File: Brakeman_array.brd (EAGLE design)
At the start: 103.1 x 99.1 mm, 56 parts

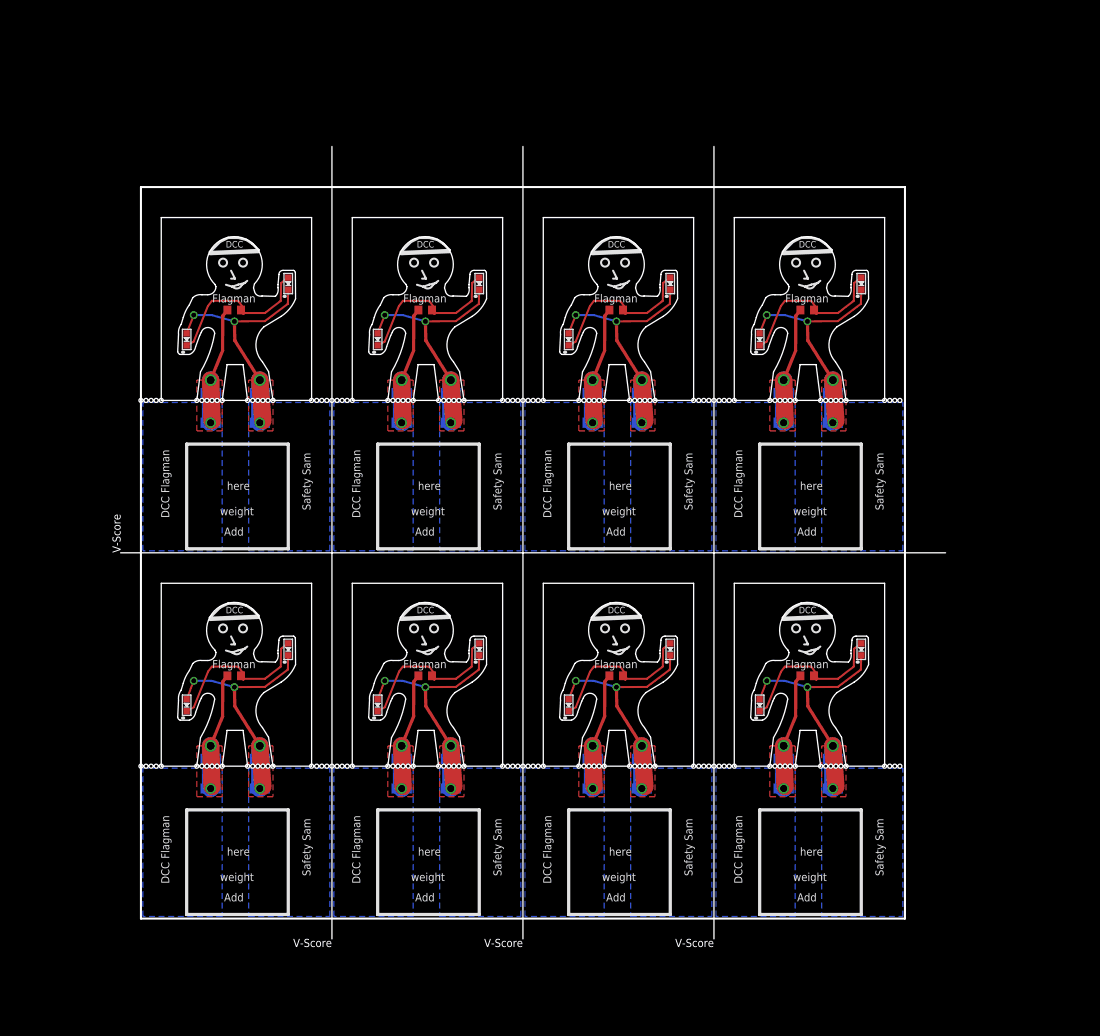
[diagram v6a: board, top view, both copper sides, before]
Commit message: Revert "Version 2.4"
This reverts commit de817f9b6bc09cb4258c25781ce6263bd1cc7bce.
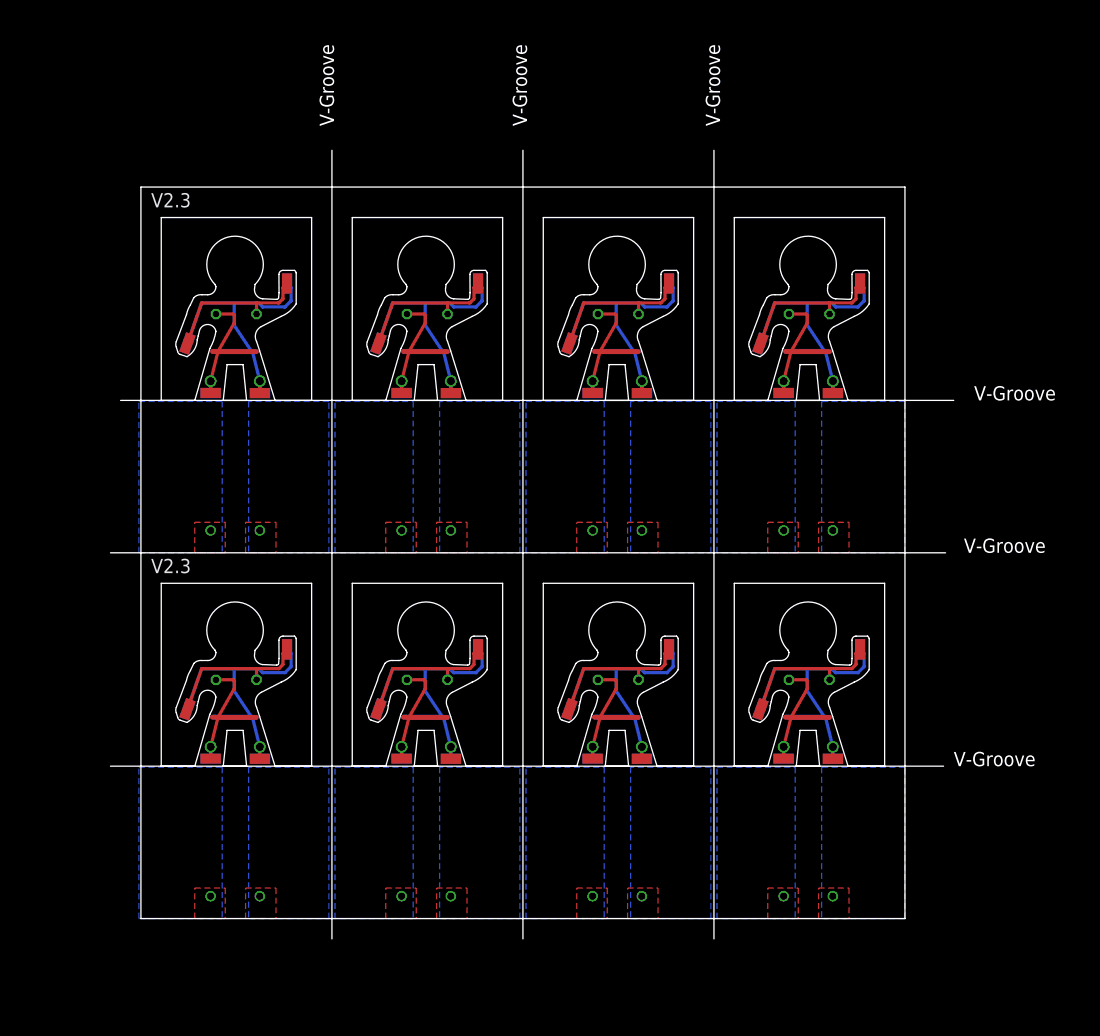
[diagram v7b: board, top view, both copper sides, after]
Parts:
- removed LED1X11, LED1X12, LED1X21, LED1X22, LED1X31, LED1X32, LED1X41, LED1X42, LED2X11, LED2X12, LED2X21, LED2X22, LED2X31, LED2X32, LED2X41, LED2X42: (no value), SPCoast:0603-LED
- removed PADNF1X11, PADNF1X12, PADNF1X21, PADNF1X22, PADNF1X31, PADNF1X32, PADNF1X41, PADNF1X42, PADNFX11, PADNFX12, PADNFX21, PADNFX22, PADNFX31, PADNFX32, PADNFX41, PADNFX42, PADSF1X11, PADSF1X12, PADSF1X21, PADSF1X22, PADSF1X31, PADSF1X32, PADSF1X41, PADSF1X42, PADSFX11, PADSFX12, PADSFX21, PADSFX22, PADSFX31, PADSFX32, PADSFX41, PADSFX42: pad, SPCoast:SMD1,27-2,54
- removed R1KX11, R1KX12, R1KX21, R1KX22, R1KX31, R1KX32, R1KX41, R1KX42: 1k0, resistor:R0603
- added PADL1, PADL10, PADL11, PADL12, PADL13, PADL14, PADL15, PADL16, PADL2, PADL3, PADL4, PADL5, PADL6, PADL7, PADL8, PADL9, PADNA, PADNA1, PADNA10, PADNA11, PADNA12, PADNA13, PADNA14, PADNA15, PADNA2, PADNA3, PADNA4, PADNA5, PADNA6, PADNA7, PADNA8, PADNA9, PADNF, PADNF1, PADNF10, PADNF11, PADNF12, PADNF13, PADNF14, PADNF15, PADNF2, PADNF3, PADNF4, PADNF5, PADNF6, PADNF7, PADNF8, PADNF9, PADSF, PADSF1, PADSF10, PADSF11, PADSF12, PADSF13, PADSF14, PADSF15, PADSF2, PADSF3, PADSF4, PADSF5, PADSF6, PADSF7, PADSF8, PADSF9: pad, wirepad:SMD1.27-2.54
- added R1, R2, R3, R4, R5, R6, R7, R8: 1k0, resistor:0204/5
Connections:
- removed net LIMITEDX11: LED1X11.C, LED2X11.A, R1KX11.1
- removed net LIMITEDX12: LED1X12.C, LED2X12.A, R1KX12.1
- removed net LIMITEDX21: LED1X21.C, LED2X21.A, R1KX21.1
- removed net LIMITEDX22: LED1X22.C, LED2X22.A, R1KX22.1
- removed net LIMITEDX31: LED1X31.C, LED2X31.A, R1KX31.1
- removed net LIMITEDX32: LED1X32.C, LED2X32.A, R1KX32.1
- removed net LIMITEDX41: LED1X41.C, LED2X41.A, R1KX41.1
- removed net LIMITEDX42: LED1X42.C, LED2X42.A, R1KX42.1
- removed net NX11: LED1X11.A, LED2X11.C, PADNF1X11.1, PADNFX11.1
- removed net NX12: LED1X12.A, LED2X12.C, PADNF1X12.1, PADNFX12.1
- removed net NX21: LED1X21.A, LED2X21.C, PADNF1X21.1, PADNFX21.1
- removed net NX22: LED1X22.A, LED2X22.C, PADNF1X22.1, PADNFX22.1
- removed net NX31: LED1X31.A, LED2X31.C, PADNF1X31.1, PADNFX31.1
- removed net NX32: LED1X32.A, LED2X32.C, PADNF1X32.1, PADNFX32.1
- removed net NX41: LED1X41.A, LED2X41.C, PADNF1X41.1, PADNFX41.1
- removed net NX42: LED1X42.A, LED2X42.C, PADNF1X42.1, PADNFX42.1
- removed net SX11: PADSF1X11.1, PADSFX11.1, R1KX11.2
- removed net SX12: PADSF1X12.1, PADSFX12.1, R1KX12.2
- removed net SX21: PADSF1X21.1, PADSFX21.1, R1KX21.2
- removed net SX22: PADSF1X22.1, PADSFX22.1, R1KX22.2
- removed net SX31: PADSF1X31.1, PADSFX31.1, R1KX31.2
- removed net SX32: PADSF1X32.1, PADSFX32.1, R1KX32.2
- removed net SX41: PADSF1X41.1, PADSFX41.1, R1KX41.2
- removed net SX42: PADSF1X42.1, PADSFX42.1, R1KX42.2
- new net LIMITED: PADL1.1, PADL2.1, R1.1
- new net LIMITED1: PADL3.1, PADL4.1, R2.1
- new net LIMITED2: PADL5.1, PADL6.1, R3.1
- new net LIMITED3: PADL7.1, PADL8.1, R4.1
- new net LIMITED4: PADL10.1, PADL9.1, R5.1
- new net LIMITED5: PADL11.1, PADL12.1, R6.1
- new net LIMITED6: PADL13.1, PADL14.1, R7.1
- new net LIMITED7: PADL15.1, PADL16.1, R8.1
- new net N: PADNA.1, PADNA2.1, PADNF.1, PADNF2.1
- new net N1: PADNA1.1, PADNA3.1, PADNF1.1, PADNF3.1
- new net N2: PADNA4.1, PADNA5.1, PADNF4.1, PADNF5.1
- new net N3: PADNA6.1, PADNA7.1, PADNF6.1, PADNF7.1
- new net N4: PADNA8.1, PADNA9.1, PADNF8.1, PADNF9.1
- new net N5: PADNA10.1, PADNA11.1, PADNF10.1, PADNF11.1
- new net N6: PADNA12.1, PADNA13.1, PADNF12.1, PADNF13.1
- new net N7: PADNA14.1, PADNA15.1, PADNF14.1, PADNF15.1
- new net S: PADSF.1, PADSF2.1, R1.2
- new net S1: PADSF1.1, PADSF3.1, R2.2
- new net S2: PADSF4.1, PADSF5.1, R3.2
- new net S3: PADSF6.1, PADSF7.1, R4.2
- new net S4: PADSF8.1, PADSF9.1, R5.2
- new net S5: PADSF10.1, PADSF11.1, R6.2
- new net S6: PADSF12.1, PADSF13.1, R7.2
- new net S7: PADSF14.1, PADSF15.1, R8.2
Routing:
- net N: track 0.00 -> 38.6 mm, vias 0 -> 2
- net N2: track 0.00 -> 38.6 mm, vias 0 -> 2
- net N4: track 0.00 -> 38.6 mm, vias 0 -> 2
- net N6: track 0.00 -> 38.6 mm, vias 0 -> 2
- net N1: track 0.00 -> 38.6 mm, vias 0 -> 2
- net N3: track 0.00 -> 38.6 mm, vias 0 -> 2
- net N5: track 0.00 -> 38.6 mm, vias 0 -> 2
- net N7: track 0.00 -> 38.6 mm, vias 0 -> 2
- net NX42: track 35.5 -> 0.00 mm, vias 4 -> 0
- net NX32: track 35.5 -> 0.00 mm, vias 4 -> 0
- net NX22: track 35.5 -> 0.00 mm, vias 4 -> 0
- net NX12: track 35.5 -> 0.00 mm, vias 4 -> 0
- net NX41: track 35.5 -> 0.00 mm, vias 4 -> 0
- net NX31: track 35.5 -> 0.00 mm, vias 4 -> 0
- net NX21: track 35.5 -> 0.00 mm, vias 4 -> 0
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- added copper zone on layer 1, net N
- added copper zone on layer 16, net N
- added copper zone on layer 1, net N1
- added copper zone on layer 16, net N1
- added copper zone on layer 1, net N2
- added copper zone on layer 16, net N2
- added copper zone on layer 1, net N3
- added copper zone on layer 16, net N3
- added copper zone on layer 1, net N4
- added copper zone on layer 16, net N4
- added copper zone on layer 1, net N5
- added copper zone on layer 16, net N5
- added copper zone on layer 1, net N6
- added copper zone on layer 16, net N6
- added copper zone on layer 1, net N7
- added copper zone on layer 16, net N7
- added copper zone on layer 1, net S
- added copper zone on layer 16, net S
- added copper zone on layer 1, net S1
- added copper zone on layer 16, net S1
- added copper zone on layer 1, net S2
- added copper zone on layer 16, net S2
- added copper zone on layer 1, net S3
- added copper zone on layer 16, net S3
- added copper zone on layer 1, net S4
- added copper zone on layer 16, net S4
- added copper zone on layer 1, net S5
- added copper zone on layer 16, net S5
- added copper zone on layer 1, net S6
- added copper zone on layer 16, net S6
- added copper zone on layer 1, net S7
- added copper zone on layer 16, net S7
- removed copper zone on layer 1, net NX11
- removed copper zone on layer 16, net NX11
- removed copper zone on layer 1, net NX12
- removed copper zone on layer 16, net NX12
- removed copper zone on layer 1, net NX21
- removed copper zone on layer 16, net NX21
- removed copper zone on layer 1, net NX22
- removed copper zone on layer 16, net NX22
- removed copper zone on layer 1, net NX31
- removed copper zone on layer 16, net NX31
- removed copper zone on layer 1, net NX32
- removed copper zone on layer 16, net NX32
- removed copper zone on layer 1, net NX41
- removed copper zone on layer 16, net NX41
- removed copper zone on layer 1, net NX42
- removed copper zone on layer 16, net NX42
- removed copper zone on layer 1, net SX11
- removed copper zone on layer 16, net SX11
- removed copper zone on layer 1, net SX12
- removed copper zone on layer 16, net SX12
- removed copper zone on layer 1, net SX21
- removed copper zone on layer 16, net SX21
- removed copper zone on layer 1, net SX22
- removed copper zone on layer 16, net SX22
- removed copper zone on layer 1, net SX31
- removed copper zone on layer 16, net SX31
- removed copper zone on layer 1, net SX32
- removed copper zone on layer 16, net SX32
- removed copper zone on layer 1, net SX41
- removed copper zone on layer 16, net SX41
- removed copper zone on layer 1, net SX42
- removed copper zone on layer 16, net SX42
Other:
- board size 103.1 x 99.1 mm -> 105.4 x 98.6 mm
- board text added: "2016.11"
- board text added: "Break off and discard"
- board text added: "V-Groove"
- board text added: "V2.3"
- board text removed: "2016.11 2024.01"
- board text removed: "John Plocher 2024.01"
- board text removed: "Safety Sam DCC Flagman"
- board text removed: "V-Score"

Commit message: added foot tiedowns
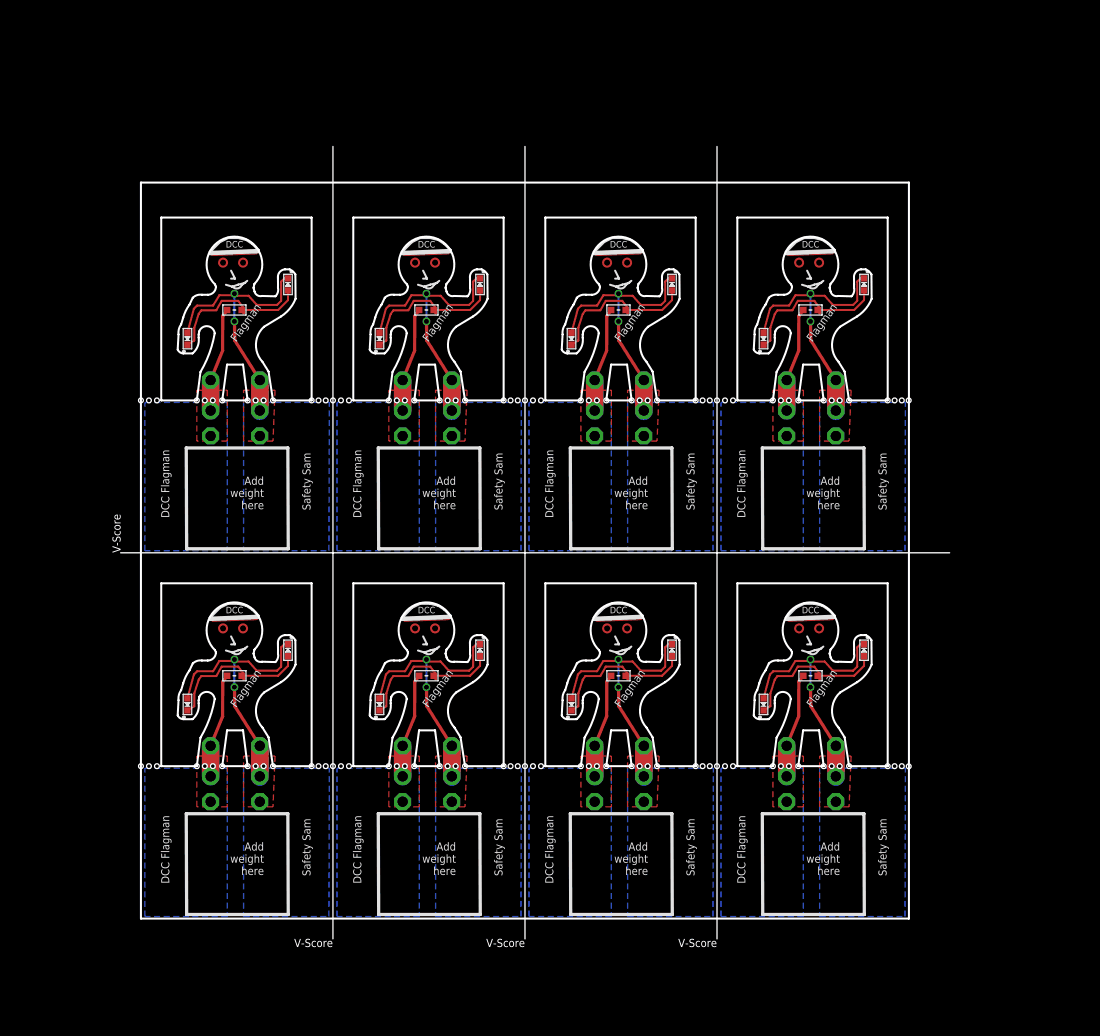
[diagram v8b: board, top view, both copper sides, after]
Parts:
- removed PADL1, PADL10, PADL11, PADL12, PADL13, PADL14, PADL15, PADL16, PADL2, PADL3, PADL4, PADL5, PADL6, PADL7, PADL8, PADL9, PADNA, PADNA1, PADNA10, PADNA11, PADNA12, PADNA13, PADNA14, PADNA15, PADNA2, PADNA3, PADNA4, PADNA5, PADNA6, PADNA7, PADNA8, PADNA9, PADNF, PADNF1, PADNF10, PADNF11, PADNF12, PADNF13, PADNF14, PADNF15, PADNF2, PADNF3, PADNF4, PADNF5, PADNF6, PADNF7, PADNF8, PADNF9, PADSF, PADSF1, PADSF10, PADSF11, PADSF12, PADSF13, PADSF14, PADSF15, PADSF2, PADSF3, PADSF4, PADSF5, PADSF6, PADSF7, PADSF8, PADSF9: pad, wirepad:SMD1.27-2.54
- removed R1, R2, R3, R4, R5, R6, R7, R8: 1k0, resistor:0204/5
- added LED1X11, LED1X12, LED1X21, LED1X22, LED1X31, LED1X32, LED1X41, LED1X42, LED2X11, LED2X12, LED2X21, LED2X22, LED2X31, LED2X32, LED2X41, LED2X42: R, SPCoast:0603-LED
- added R1KX11, R1KX12, R1KX21, R1KX22, R1KX31, R1KX32, R1KX41, R1KX42: 1k0, SPCoast:0603-RES
- added TP1X11, TP1X12, TP1X21, TP1X22, TP1X31, TP1X32, TP1X41, TP1X42, TP2X11, TP2X12, TP2X21, TP2X22, TP2X31, TP2X32, TP2X41, TP2X42, TP3X11, TP3X12, TP3X21, TP3X22, TP3X31, TP3X32, TP3X41, TP3X42, TP4X11, TP4X12, TP4X21, TP4X22, TP4X31, TP4X32, TP4X41, TP4X42, TP5X11, TP5X12, TP5X21, TP5X22, TP5X31, TP5X32, TP5X41, TP5X42, TP6X11, TP6X12, TP6X21, TP6X22, TP6X31, TP6X32, TP6X41, TP6X42: PTR1PAD1-13, testpad:P1-13
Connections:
- removed net LIMITED: PADL1.1, PADL2.1, R1.1
- removed net LIMITED1: PADL3.1, PADL4.1, R2.1
- removed net LIMITED2: PADL5.1, PADL6.1, R3.1
- removed net LIMITED3: PADL7.1, PADL8.1, R4.1
- removed net LIMITED4: PADL10.1, PADL9.1, R5.1
- removed net LIMITED5: PADL11.1, PADL12.1, R6.1
- removed net LIMITED6: PADL13.1, PADL14.1, R7.1
- removed net LIMITED7: PADL15.1, PADL16.1, R8.1
- removed net N: PADNA.1, PADNA2.1, PADNF.1, PADNF2.1
- removed net N1: PADNA1.1, PADNA3.1, PADNF1.1, PADNF3.1
- removed net N2: PADNA4.1, PADNA5.1, PADNF4.1, PADNF5.1
- removed net N3: PADNA6.1, PADNA7.1, PADNF6.1, PADNF7.1
- removed net N4: PADNA8.1, PADNA9.1, PADNF8.1, PADNF9.1
- removed net N5: PADNA10.1, PADNA11.1, PADNF10.1, PADNF11.1
- removed net N6: PADNA12.1, PADNA13.1, PADNF12.1, PADNF13.1
- removed net N7: PADNA14.1, PADNA15.1, PADNF14.1, PADNF15.1
- removed net S: PADSF.1, PADSF2.1, R1.2
- removed net S1: PADSF1.1, PADSF3.1, R2.2
- removed net S2: PADSF4.1, PADSF5.1, R3.2
- removed net S3: PADSF6.1, PADSF7.1, R4.2
- removed net S4: PADSF8.1, PADSF9.1, R5.2
- removed net S5: PADSF10.1, PADSF11.1, R6.2
- removed net S6: PADSF12.1, PADSF13.1, R7.2
- removed net S7: PADSF14.1, PADSF15.1, R8.2
- new net LIMITEDX11: LED1X11.C, LED2X11.A, R1KX11.1
- new net LIMITEDX12: LED1X12.C, LED2X12.A, R1KX12.1
- new net LIMITEDX21: LED1X21.C, LED2X21.A, R1KX21.1
- new net LIMITEDX22: LED1X22.C, LED2X22.A, R1KX22.1
- new net LIMITEDX31: LED1X31.C, LED2X31.A, R1KX31.1
- new net LIMITEDX32: LED1X32.C, LED2X32.A, R1KX32.1
- new net LIMITEDX41: LED1X41.C, LED2X41.A, R1KX41.1
- new net LIMITEDX42: LED1X42.C, LED2X42.A, R1KX42.1
- new net NX11: LED1X11.A, LED2X11.C, TP3X11.TP, TP4X11.TP, TP6X11.TP
- new net NX12: LED1X12.A, LED2X12.C, TP3X12.TP, TP4X12.TP, TP6X12.TP
- new net NX21: LED1X21.A, LED2X21.C, TP3X21.TP, TP4X21.TP, TP6X21.TP
- new net NX22: LED1X22.A, LED2X22.C, TP3X22.TP, TP4X22.TP, TP6X22.TP
- new net NX31: LED1X31.A, LED2X31.C, TP3X31.TP, TP4X31.TP, TP6X31.TP
- new net NX32: LED1X32.A, LED2X32.C, TP3X32.TP, TP4X32.TP, TP6X32.TP
- new net NX41: LED1X41.A, LED2X41.C, TP3X41.TP, TP4X41.TP, TP6X41.TP
- new net NX42: LED1X42.A, LED2X42.C, TP3X42.TP, TP4X42.TP, TP6X42.TP
- new net SX11: R1KX11.2, TP1X11.TP, TP2X11.TP, TP5X11.TP
- new net SX12: R1KX12.2, TP1X12.TP, TP2X12.TP, TP5X12.TP
- new net SX21: R1KX21.2, TP1X21.TP, TP2X21.TP, TP5X21.TP
- new net SX22: R1KX22.2, TP1X22.TP, TP2X22.TP, TP5X22.TP
- new net SX31: R1KX31.2, TP1X31.TP, TP2X31.TP, TP5X31.TP
- new net SX32: R1KX32.2, TP1X32.TP, TP2X32.TP, TP5X32.TP
- new net SX41: R1KX41.2, TP1X41.TP, TP2X41.TP, TP5X41.TP
- new net SX42: R1KX42.2, TP1X42.TP, TP2X42.TP, TP5X42.TP
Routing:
- net NX42: track 0.00 -> 38.6 mm, vias 0 -> 2
- net NX32: track 0.00 -> 38.6 mm, vias 0 -> 2
- net NX22: track 0.00 -> 38.6 mm, vias 0 -> 2
- net NX12: track 0.00 -> 38.6 mm, vias 0 -> 2
- net NX41: track 0.00 -> 38.6 mm, vias 0 -> 2
- net NX31: track 0.00 -> 38.6 mm, vias 0 -> 2
- net NX21: track 0.00 -> 38.6 mm, vias 0 -> 2
- net NX11: track 0.00 -> 38.6 mm, vias 0 -> 2
- net N: track 38.6 -> 0.00 mm, vias 2 -> 0
- net N2: track 38.6 -> 0.00 mm, vias 2 -> 0
- net N4: track 38.6 -> 0.00 mm, vias 2 -> 0
- net N6: track 38.6 -> 0.00 mm, vias 2 -> 0
- net N1: track 38.6 -> 0.00 mm, vias 2 -> 0
- net N3: track 38.6 -> 0.00 mm, vias 2 -> 0
- net N5: track 38.6 -> 0.00 mm, vias 2 -> 0
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- added copper zone on layer 1, net NX11
- added copper zone on layer 16, net NX11
- added copper zone on layer 1, net NX12
- added copper zone on layer 16, net NX12
- added copper zone on layer 1, net NX21
- added copper zone on layer 16, net NX21
- added copper zone on layer 1, net NX22
- added copper zone on layer 16, net NX22
- added copper zone on layer 1, net NX31
- added copper zone on layer 16, net NX31
- added copper zone on layer 1, net NX32
- added copper zone on layer 16, net NX32
- added copper zone on layer 1, net NX41
- added copper zone on layer 16, net NX41
- added copper zone on layer 1, net NX42
- added copper zone on layer 16, net NX42
- added copper zone on layer 1, net SX11
- added copper zone on layer 16, net SX11
- added copper zone on layer 1, net SX12
- added copper zone on layer 16, net SX12
- added copper zone on layer 1, net SX21
- added copper zone on layer 16, net SX21
- added copper zone on layer 1, net SX22
- added copper zone on layer 16, net SX22
- added copper zone on layer 1, net SX31
- added copper zone on layer 16, net SX31
- added copper zone on layer 1, net SX32
- added copper zone on layer 16, net SX32
- added copper zone on layer 1, net SX41
- added copper zone on layer 16, net SX41
- added copper zone on layer 1, net SX42
- added copper zone on layer 16, net SX42
- removed copper zone on layer 1, net N
- removed copper zone on layer 16, net N
- removed copper zone on layer 1, net N1
- removed copper zone on layer 16, net N1
- removed copper zone on layer 1, net N2
- removed copper zone on layer 16, net N2
- removed copper zone on layer 1, net N3
- removed copper zone on layer 16, net N3
- removed copper zone on layer 1, net N4
- removed copper zone on layer 16, net N4
- removed copper zone on layer 1, net N5
- removed copper zone on layer 16, net N5
- removed copper zone on layer 1, net N6
- removed copper zone on layer 16, net N6
- removed copper zone on layer 1, net N7
- removed copper zone on layer 16, net N7
- removed copper zone on layer 1, net S
- removed copper zone on layer 16, net S
- removed copper zone on layer 1, net S1
- removed copper zone on layer 16, net S1
- removed copper zone on layer 1, net S2
- removed copper zone on layer 16, net S2
- removed copper zone on layer 1, net S3
- removed copper zone on layer 16, net S3
- removed copper zone on layer 1, net S4
- removed copper zone on layer 16, net S4
- removed copper zone on layer 1, net S5
- removed copper zone on layer 16, net S5
- removed copper zone on layer 1, net S6
- removed copper zone on layer 16, net S6
- removed copper zone on layer 1, net S7
- removed copper zone on layer 16, net S7
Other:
- board size 105.4 x 98.6 mm -> 103.6 x 99.1 mm
- board text added: "2016.11 2024.01"
- board text added: "Add weight here"
- board text added: "John Plocher 2024.01"
- board text added: "Safety Sam DCC Flagman"
- board text added: "V-Score"
- board text removed: "2016.11"
- board text removed: "Add"
- board text removed: "Break off and discard"
- board text removed: "V-Groove"
- board text removed: "V2.3"
- board text removed: "here"
- board text removed: "weight"
